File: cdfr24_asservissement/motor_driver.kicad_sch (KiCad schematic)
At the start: 21 parts

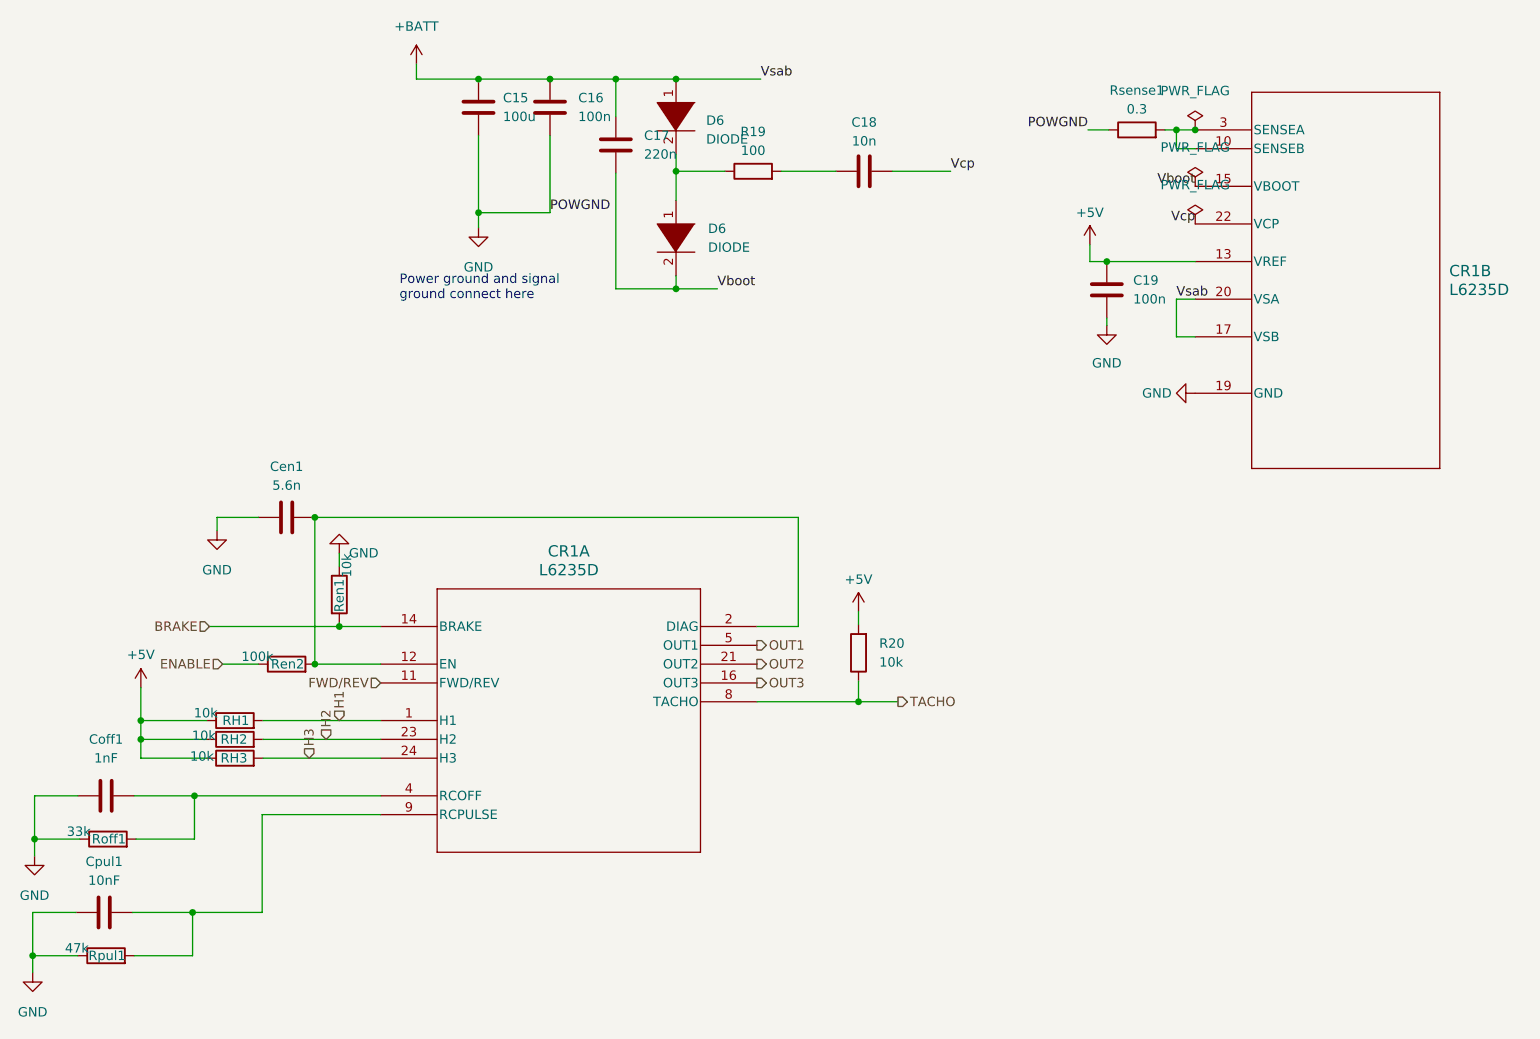
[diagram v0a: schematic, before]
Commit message: Add new components
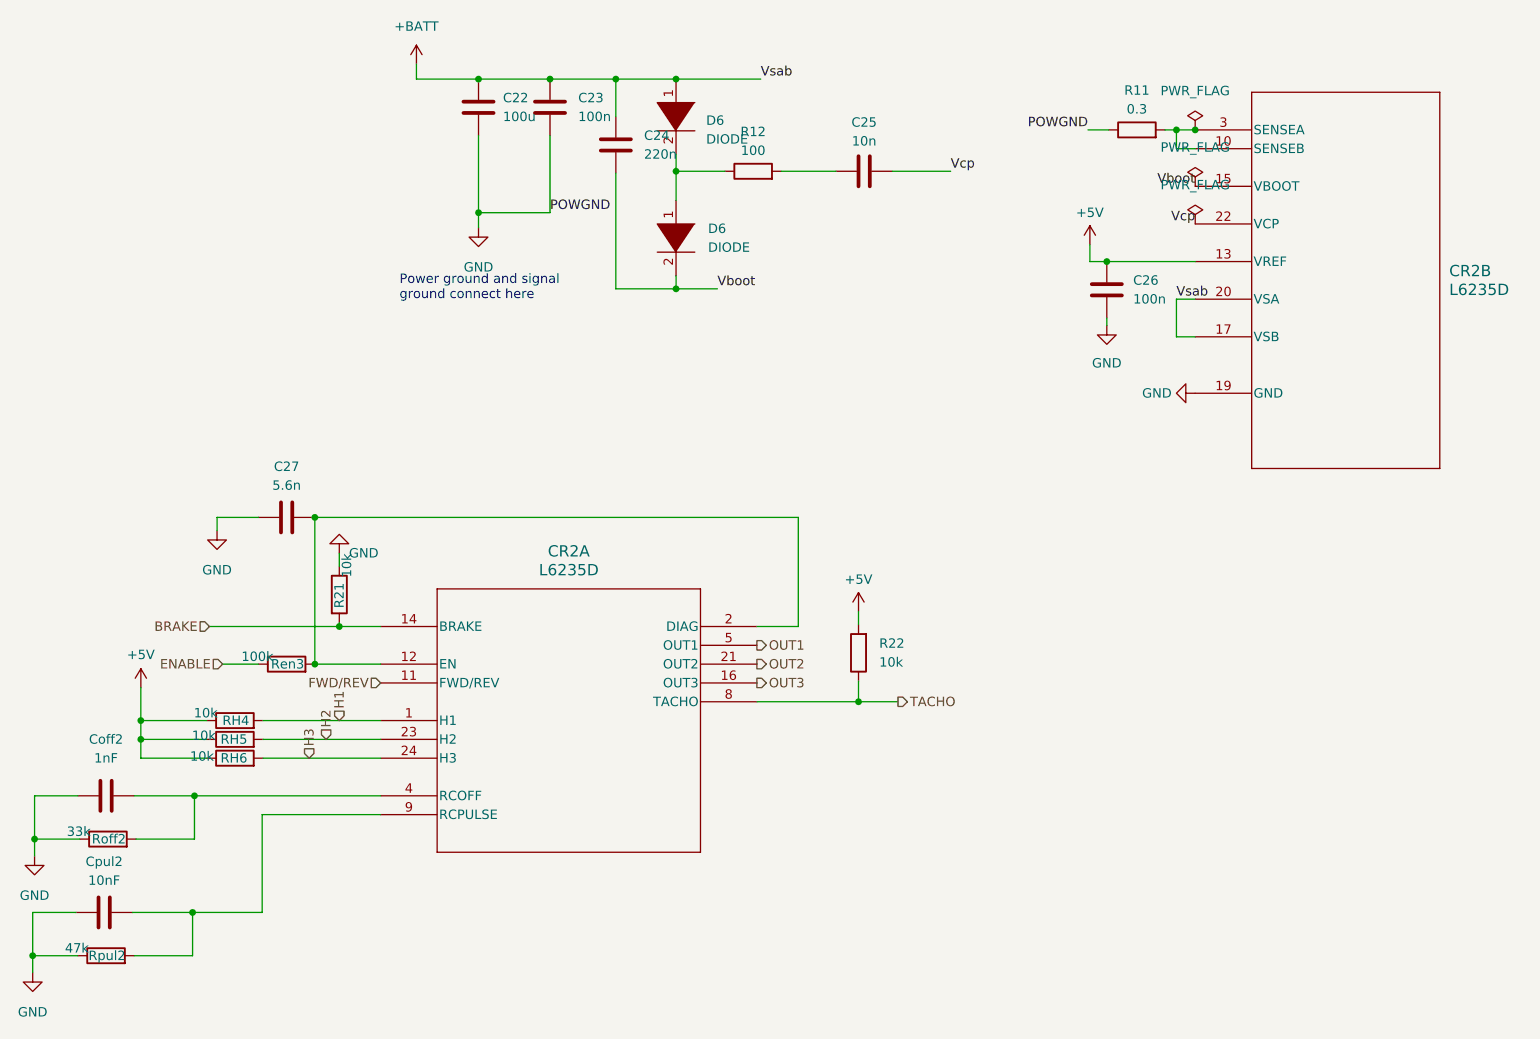
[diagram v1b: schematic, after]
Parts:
- renumbered C15 to C22, C16 to C23, C17 to C24, C18 to C25, C19 to C26, Cen1 to C27, CR1 to CR2, Coff1 to Coff2, Cpul1 to Cpul2, Rsense1 to R11, R19 to R12, Ren1 to R21, R20 to R22, RH1 to RH4, RH2 to RH5, RH3 to RH6, Ren2 to Ren3, Roff1 to Roff2, Rpul1 to Rpul2
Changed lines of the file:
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@@
 		(dnp no)
 		(fields_autoplaced yes)
-		(property "Reference" "#PWR040"
+		(property "Reference" "#PWR053"
 			(at 142.748 52.832 0)
 			(effects
@@
 		(dnp no)
 		(fields_autoplaced yes)
-		(property "Reference" "#PWR016"
+		(property "Reference" "#PWR022"
 			(at 233.172 68.834 0)
 			(effects
@@
 		(dnp no)
 		(fields_autoplaced yes)
-		(property "Reference" "C15"
+		(property "Reference" "C22"
 			(at 146.05 28.956 0)
 			(effects
@@
 		(on_board yes)
 		(dnp no)
-		(property "Reference" "RH3"
+		(property "Reference" "RH6"
 			(at 109.728 118.11 90)
 			(effects
@@
 		(dnp no)
 		(fields_autoplaced yes)
-		(property "Reference" "CR1"
+		(property "Reference" "CR2"
 			(at 154.94 90.17 0)
 			(effects
@@
 		(dnp no)
 		(fields_autoplaced yes)
-		(property "Reference" "CR1"
+		(property "Reference" "CR2"
 			(at 273.812 52.324 0)
 			(effects
@@
 		(dnp no)
 		(fields_autoplaced yes)
-		(property "Reference" "Cpul1"
+		(property "Reference" "Cpul2"
 			(at 92.202 132.08 90)
 			(effects
@@
 		(dnp no)
 		(fields_autoplaced yes)
-		(property "Reference" "#PWR044"
+		(property "Reference" "#PWR057"
 			(at 107.442 93.726 0)
 			(effects
@@
 		(on_board yes)
 		(dnp no)
-		(property "Reference" "Ren1"
+		(property "Reference" "R21"
 			(at 123.952 96.139 90)
 			(effects
@@
 		(on_board yes)
 		(dnp no)
-		(property "Reference" "RH1"
+		(property "Reference" "RH4"
 			(at 109.982 113.03 90)
 			(effects
@@
 		(on_board yes)
 		(dnp no)
-		(property "Reference" "Roff1"
+		(property "Reference" "Roff2"
 			(at 92.837 129.032 90)
 			(effects
@@
 		(dnp no)
 		(fields_autoplaced yes)
-		(property "Reference" "Coff1"
+		(property "Reference" "Coff2"
 			(at 92.456 115.57 90)
 			(effects
@@
 		(dnp no)
 		(fields_autoplaced yes)
-		(property "Reference" "C18"
+		(property "Reference" "C25"
 			(at 194.818 32.258 90)
 			(effects
@@
 		(dnp no)
 		(fields_autoplaced yes)
-		(property "Reference" "R19"
+		(property "Reference" "R12"
 			(at 179.832 33.528 90)
 			(effects
@@
 		(on_board yes)
 		(dnp no)
-		(property "Reference" "Rpul1"
+		(property "Reference" "Rpul2"
 			(at 92.583 144.78 90)
 			(effects
@@
 		(dnp no)
 		(fields_autoplaced yes)
-		(property "Reference" "C17"
+		(property "Reference" "C24"
 			(at 165.1 34.036 0)
 			(effects
@@
 		(dnp no)
 		(fields_autoplaced yes)
-		(property "Reference" "C16"
+		(property "Reference" "C23"
 			(at 156.21 28.956 0)
 			(effects
@@
 		(dnp no)
 		(fields_autoplaced yes)
-		(property "Reference" "R20"
+		(property "Reference" "R22"
 			(at 196.85 102.616 0)
 			(effects
@@
 		(on_board yes)
 		(dnp no)
-		(property "Reference" "#PWR045"
+		(property "Reference" "#PWR058"
 			(at 123.952 84.074 0)
 			(effects
@@
 		(dnp no)
 		(fields_autoplaced yes)
-		(property "Reference" "Rsense1"
+		(property "Reference" "R11"
 			(at 231.648 27.94 90)
 			(effects
@@
 		(dnp no)
 		(fields_autoplaced yes)
-		(property "Reference" "#PWR049"
+		(property "Reference" "#PWR064"
 			(at 82.55 153.416 0)
 			(effects
@@
 		(dnp no)
 		(fields_autoplaced yes)
-		(property "Reference" "#PWR046"
+		(property "Reference" "#PWR059"
 			(at 194.056 102.108 0)
 			(effects
@@
 		(on_board yes)
 		(dnp no)
-		(property "Reference" "Ren2"
+		(property "Reference" "Ren3"
 			(at 116.967 105.41 90)
 			(effects
@@
 		(dnp no)
 		(fields_autoplaced yes)
-		(property "Reference" "#PWR047"
+		(property "Reference" "#PWR060"
 			(at 97.155 112.395 0)
 			(effects
@@
 		(dnp no)
 		(fields_autoplaced yes)
-		(property "Reference" "#FLG07"
+		(property "Reference" "#FLG08"
 			(at 239.522 38.989 0)
 			(effects
@@
 		(dnp no)
 		(fields_autoplaced yes)
-		(property "Reference" "Cen1"
+		(property "Reference" "C27"
 			(at 116.84 78.74 90)
 			(effects
@@
 		(dnp no)
 		(fields_autoplaced yes)
-		(property "Reference" "#PWR048"
+		(property "Reference" "#PWR063"
 			(at 82.804 137.668 0)
 			(effects
@@
 		(dnp no)
 		(fields_autoplaced yes)
-		(property "Reference" "#FLG09"
+		(property "Reference" "#FLG010"
 			(at 239.522 44.069 0)
 			(effects
@@
 		(dnp no)
 		(fields_autoplaced yes)
-		(property "Reference" "C19"
+		(property "Reference" "C26"
 			(at 231.14 53.594 0)
 			(effects
@@
 		(dnp no)
 		(fields_autoplaced yes)
-		(property "Reference" "#PWR041"
+		(property "Reference" "#PWR054"
 			(at 225.298 52.578 0)
 			(effects
@@
 		(dnp no)
 		(fields_autoplaced yes)
-		(property "Reference" "#FLG05"
+		(property "Reference" "#FLG06"
 			(at 239.5154 31.369 0)
 			(effects
@@
 		(dnp no)
 		(fields_autoplaced yes)
-		(property "Reference" "#PWR042"
+		(property "Reference" "#PWR055"
 			(at 227.584 66.04 0)
 			(effects
@@
 		(on_board yes)
 		(dnp no)
-		(property "Reference" "RH2"
+		(property "Reference" "RH5"
 			(at 109.728 115.57 90)
 			(effects

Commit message: Realign elements to grid
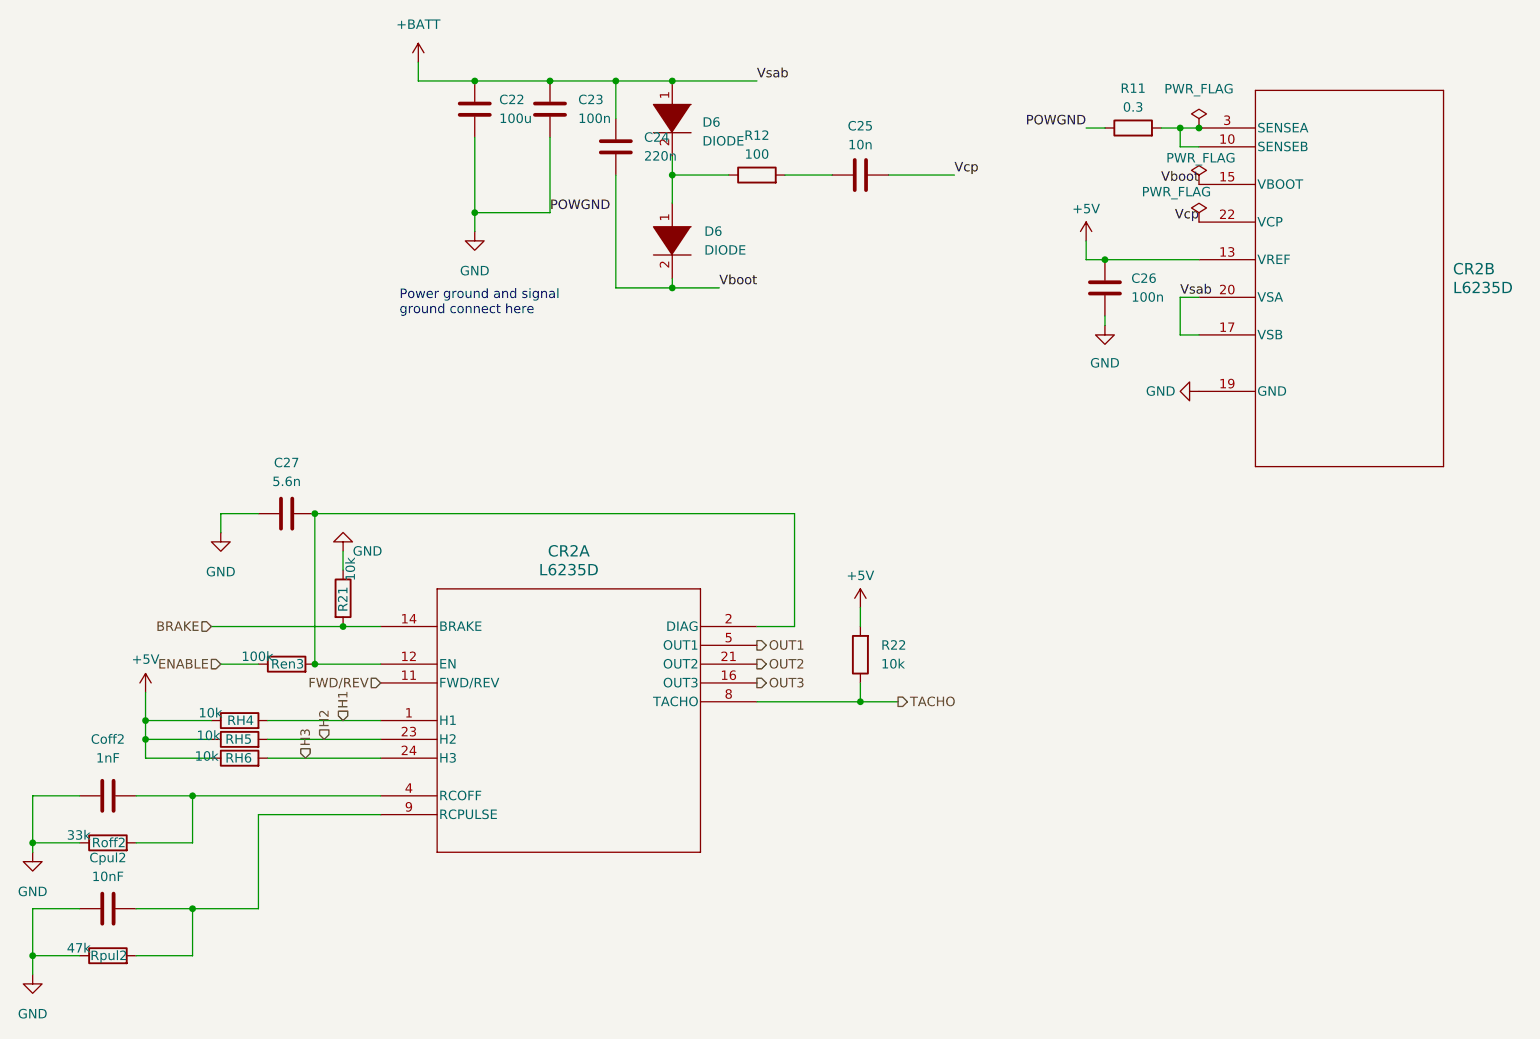
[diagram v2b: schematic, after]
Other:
- moved on the sheet: C22, C25, C27, CR2B, Cpul2, D6, R11, R12, R21, RH4, RH5, RH6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

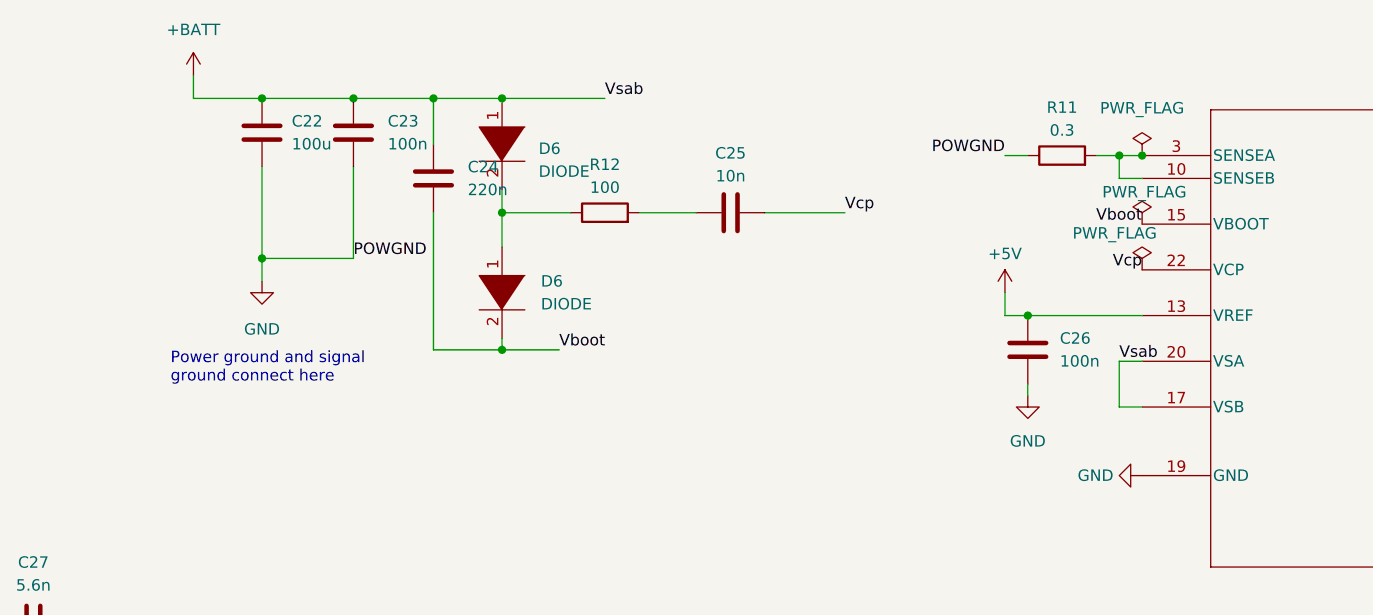
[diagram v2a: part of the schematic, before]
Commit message: Combine charge pump
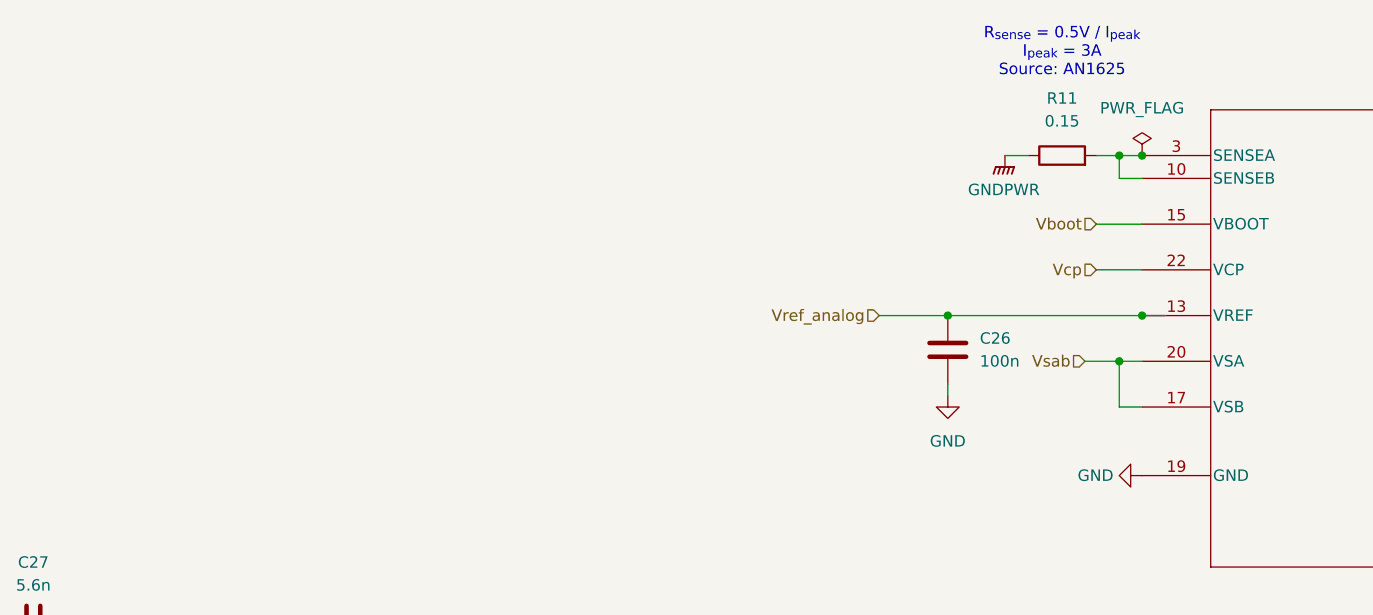
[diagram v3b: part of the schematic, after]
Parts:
- removed C22: 100u, Capacitor_SMD:CP_Elec_10x10.5, symbol Device:C
- removed C23: 100n, Capacitor_SMD:C_0805_2012Metric_Pad1.18x1.45mm_HandSolder, symbol Device:C
- removed C24: 220n, Capacitor_SMD:C_0805_2012Metric_Pad1.18x1.45mm_HandSolder, symbol Device:C
- removed C25: 10n, Capacitor_SMD:C_0805_2012Metric_Pad1.18x1.45mm_HandSolder, symbol Device:C
- removed D6 (x2): DIODE, B170B:DIOM505270X240, symbol pspice:DIODE
- removed R12: 100, Resistor_SMD:R_0805_2012Metric_Pad1.20x1.40mm_HandSolder, symbol Device:R
- R11: value 0.3 -> 0.15
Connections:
- net +5V: no longer C26.1, CR2.13 (VREF)
- net GND: no longer R11.1
- net +BATT renamed Vsab
- new net GNDPWR: R11.1
- new net Vref_analog: C26.1, CR2.13 (VREF)
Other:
- note added: "R_{sense} = 0.5V / I_{peak} I_{peak} = 3A Source: AN1625"
- note removed: "Power ground and signal ground connect here"
- moved on the sheet: C26
